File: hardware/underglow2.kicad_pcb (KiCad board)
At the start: 4 copper layers, 78.5 x 95 mm, 157 parts, among them J101 J_Delphi_Sicma_24, J501 Conn_ARM_SWD_TagConnect_TC203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, J502 Conn_ARM_SWD_TagConnect_TC2030, J503 BOOT0, J601 Conn_ARM_SWD_TagConnect_TC203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, Q301 AO4803A, Q302 8205A, Q303 8205A, Q304 8205A, Q305 BC817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

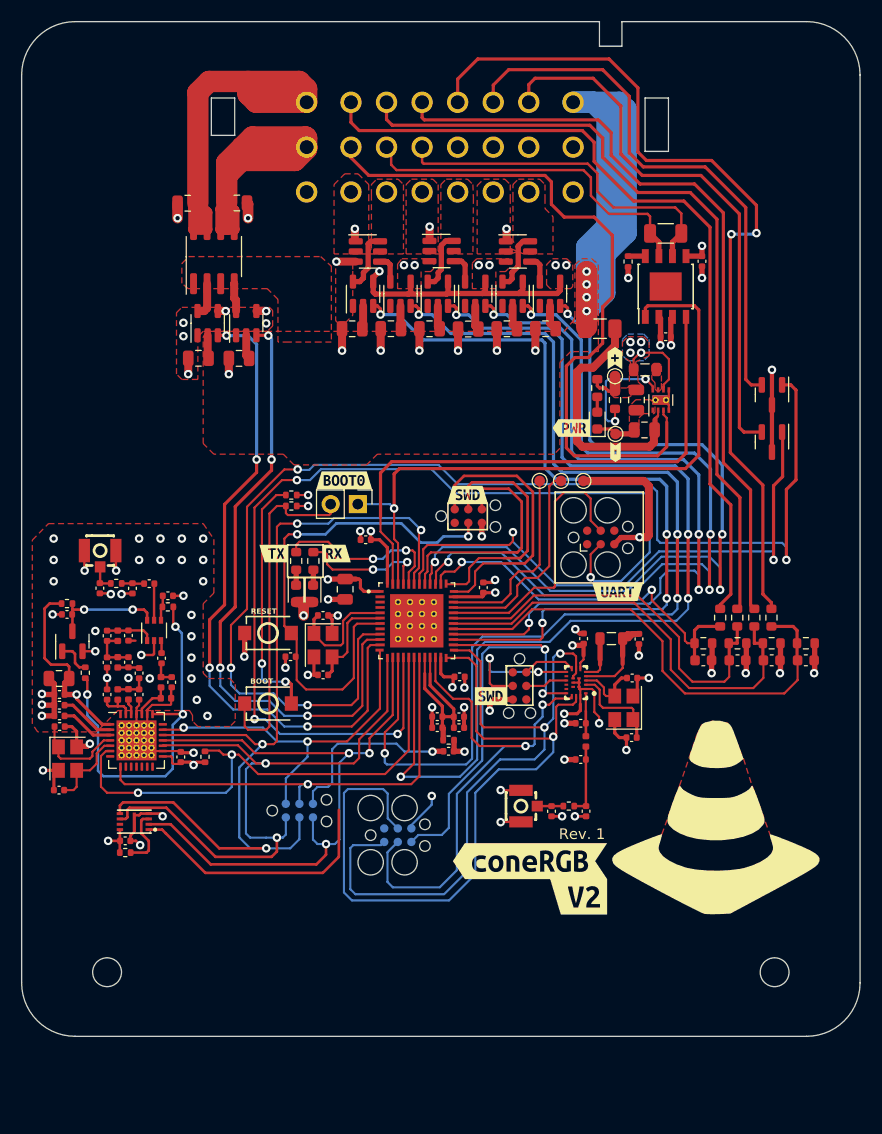
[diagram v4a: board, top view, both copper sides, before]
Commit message: hardware: add USB for debugging and programming
Signed-off-by: Connor Rigby <connorr@hey.com>
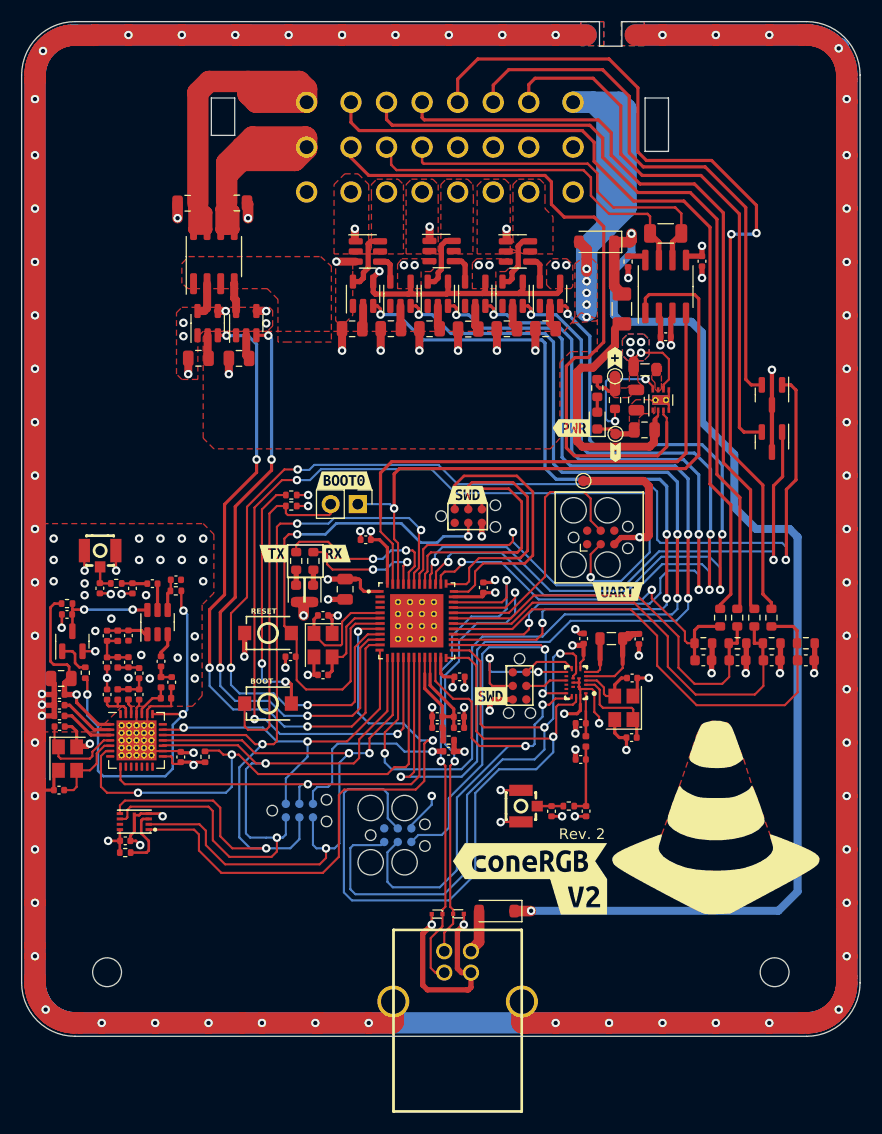
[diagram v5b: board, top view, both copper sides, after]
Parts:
- removed TP501: DP, TestPoint:TestPoint_Pad_D1.0mm
- removed TP502: DN, TestPoint:TestPoint_Pad_D1.0mm
- added D202: D_Small, Diode_SMD:D_SOD-123, F.Cu at (78.8, 45.6)
- added D203: D_Small, Diode_SMD:D_SOD-123, F.Cu at (69.5, 108.3)
- added D503: ESD9B3_3ST5G, LCSC_ESD:SOD-923_L0.8-W0.6-LS1.0-BI-1, F.Cu at (63.9, 108.6)
- added D504: ESD9B3_3ST5G, LCSC_ESD:SOD-923_L0.8-W0.6-LS1.0-BI-1, F.Cu at (65.9, 108.5)
- added J504: USB_B, LCSC_Connector:USB-B-TH_67068-8000, F.Cu at (65.8, 114.4)
- U401: footprint Package_SO:Infineon_PG-DSO-8-43 -> Package_SO:SOIC-8_3.9x4.9mm_P1.27mm
- U802: footprint Package_TO_SOT_SMD:SOT-363_SC-70-6 -> Package_TO_SOT_SMD:SOT-23-6
- moved F201 2.76 mm to (81.2, 51.9), turned to -90 degrees
- moved C829 1.68 mm to (39.4, 77.3)
- moved R803 1.68 mm to (39.4, 78.3)
- moved U802 0.84 mm to (37.7, 81.2)
- moved C823 0.30 mm to (38.0, 84.9)
- moved C825 0.30 mm to (37.2, 77.6)
- moved C816 0.20 mm to (28.7, 86.5)
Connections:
- net Net-(U502-WP#) renamed /Application/~{WP}
- F201 pad 1: +12V -> Net-(D202-K)
- U501 pad 8: unconnected-(U501-PA0-Pad8) -> /Application/SPI1_FLASH_NSS
- U502 pad 1: unconnected-(U502-CS#-Pad1) -> /Application/SPI1_FLASH_NSS
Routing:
- net GND: track 204.7 -> 873.4 mm, vias 99 -> 161
- net Net-(D202-K): track 0.00 -> 109.9 mm, vias 0 -> 2
- net /Application/SPI1_FLASH_NSS: track 0.00 -> 57.6 mm, vias 0 -> 2
- net /Application/USB_DP: track 18.2 -> 49.6 mm, vias 0 -> 2
- net /Application/USB_DN: track 19.9 -> 45.8 mm, vias 0 -> 2
- net unconnected-(U502-CS#-Pad1): track 24.5 -> 0.00 mm
- net +12V: track 71.3 -> 60.5 mm, vias 4 -> 5
- net +5V: track 0.00 -> 4.08 mm
- net /Application/CAN_RX: track 63.0 -> 65.0 mm
- net +3.3V: track 280.0 -> 278.2 mm
- net /Application/SPI1_MOSI: track 85.3 -> 87.0 mm
- net /Application/SPI1_SCK: track 62.5 -> 64.1 mm
- net /Application/DI1_TTL: track 45.5 -> 47.1 mm
- net /Radio/RXTX: track 35.5 -> 37.0 mm
- net /Application/SPI1_MISO: track 62.6 -> 64.0 mm
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- added copper zone on B.Cu, net GND
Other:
- board text added: "Rev. 2"
- board text removed: "Rev. 1"
